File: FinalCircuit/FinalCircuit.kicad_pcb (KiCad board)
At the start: 2 copper layers, 163.3 x 78.7 mm, 54 parts, among them J1 Conn_02x20_Odd_Even, J2 Conn_02x05_Odd_Even, J3 Conn_01x06, U1 LM6172, U10 CD4066BE, U11 CD4066BE, U2 OPA2277, U3 MCP3008, U4 MCP4921, U5 CD4066BE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

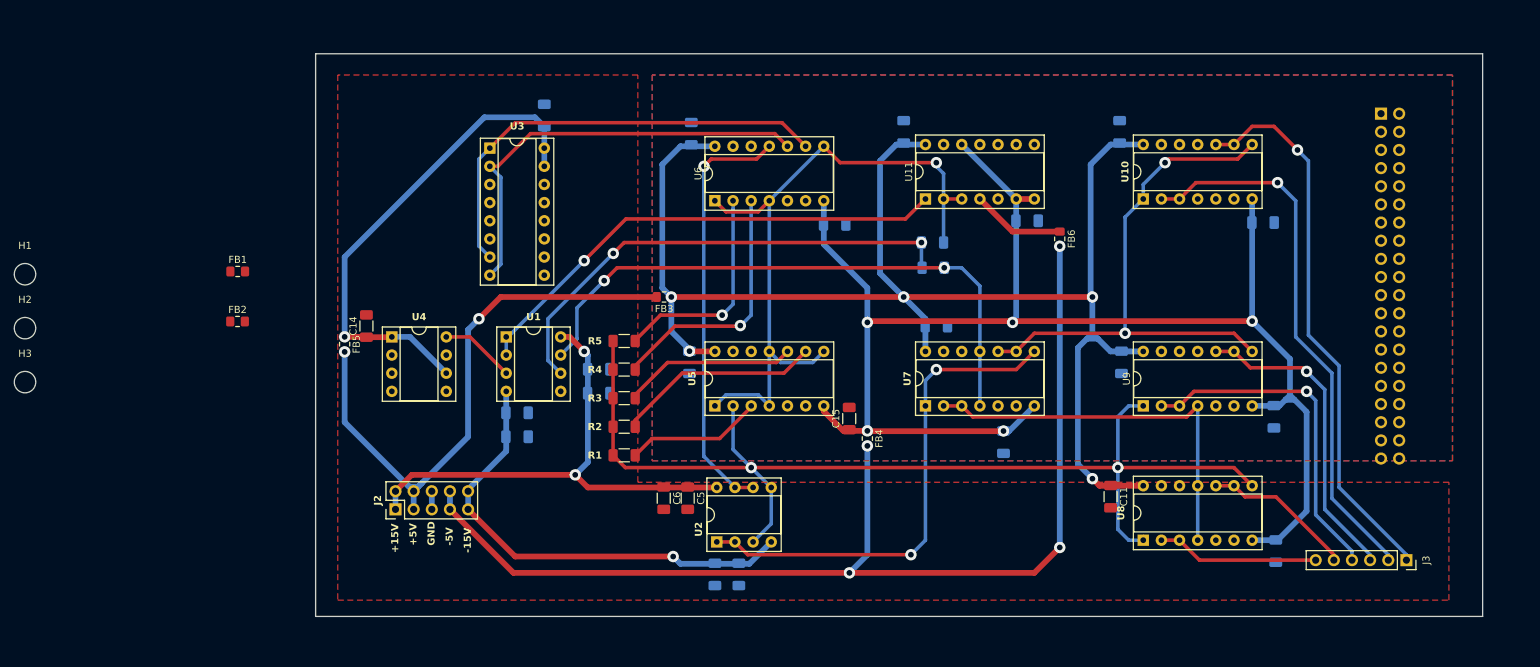
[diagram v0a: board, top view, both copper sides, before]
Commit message: Almost all connections done. Digital traces seem too long at the moment.
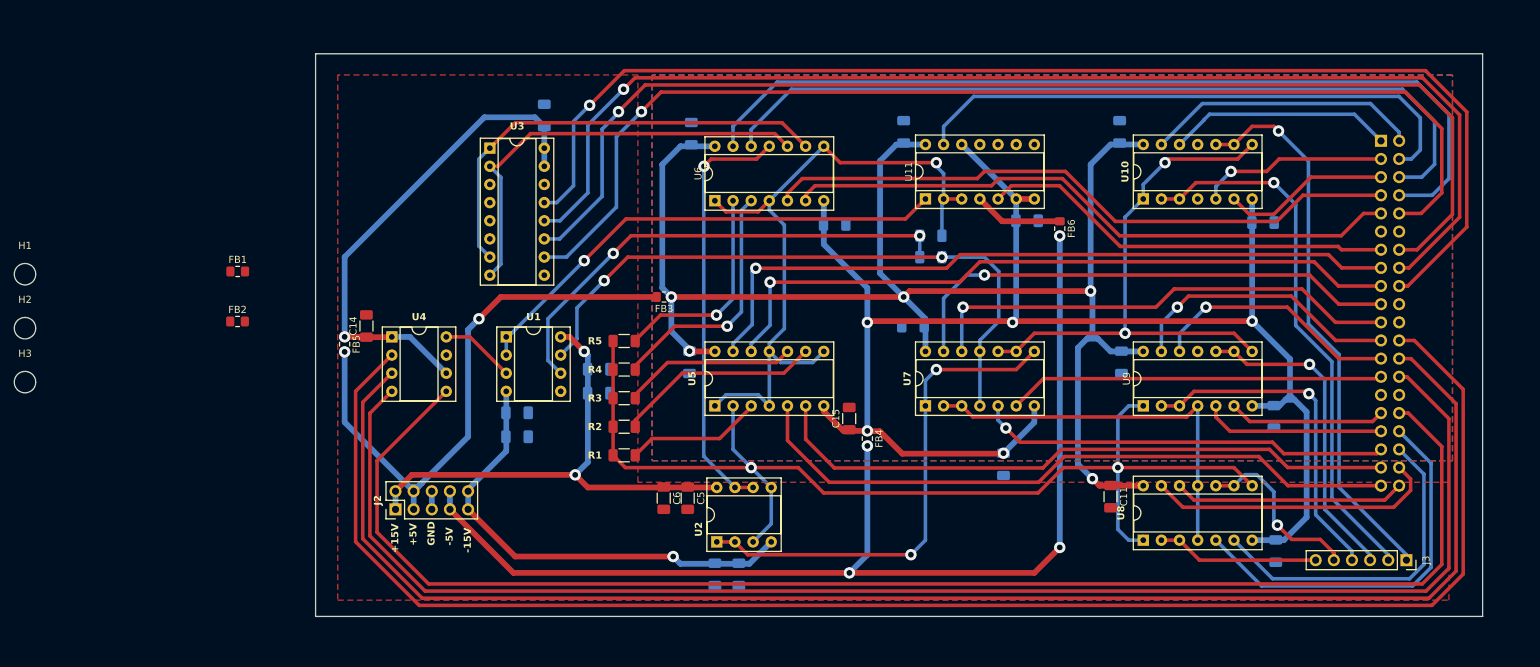
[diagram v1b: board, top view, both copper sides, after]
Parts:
- moved J1 3.80 mm to (238.0, 46.2)
- moved C9 3.27 mm to (172.5, 72.1), turned to 180 degrees
- moved C10 3.11 mm to (185.2, 91.5)
- moved R11 1.52 mm to (175.0, 62.5)
- moved FB6 1.44 mm to (193.0, 58.5)
- moved R10 0.98 mm to (175.0, 59.5)
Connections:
- J1 pad 1: /DAC_CSbar -> /Control_Vt2B
- J1 pad 10: /Control4 -> /ADC_CSbar
- J1 pad 13: /Control9A -> /ControlMain_Reset
- J1 pad 14: /Control5 -> /Din
- J1 pad 15: /Control10B -> /Control1
- J1 pad 16: /Control6 -> /Dout
- J1 pad 17: /Control9B -> /Control4
- J1 pad 18: /Control_Vt1A -> /CLK
- J1 pad 19: /Control10A -> /Control9A
- J1 pad 2: /SCK -> /Control_Vt1A
- J1 pad 20: /Control_Vt1B -> unconnected-(J1-Pin_20-Pad20)
- J1 pad 21: /Control_Hz1A -> /Control10B
- J1 pad 22: /Control_Vt2A -> unconnected-(J1-Pin_22-Pad22)
- J1 pad 23: /Control_Hz1B -> /Control_Hz3A
- J1 pad 24: /Control_Vt2B -> /DAC_CSbar
- J1 pad 25: /Control_Hz2A -> /Control_Vt3B
- J1 pad 26: /Control_Vt3A -> /SCK
- J1 pad 27: /Control_Hz2B -> /Control10A
- J1 pad 28: /Control_Vt3B -> /SDI
- J1 pad 3: /LDACbar -> /Control_Vt1B
- J1 pad 31: /Control_Hz3A -> /Control_Vt3A
- J1 pad 32: /Dout -> /LDACbar
- J1 pad 34: /ADC_CSbar -> /Control_Hz1B
- J1 pad 35: /ControlMain_ReadWrite -> /Control9B
- J1 pad 36: /Din -> /Control_Hz2A
- J1 pad 37: /ControlMain_Reset -> /Control3
- J1 pad 38: unconnected-(J1-Pin_38-Pad38) -> /Control_Hz1A
- J1 pad 39: /CLK -> /Control2
- J1 pad 4: /SDI -> /ControlMain_ReadWrite
- J1 pad 40: unconnected-(J1-Pin_40-Pad40) -> /Control_Hz2B
- J1 pad 5: /Control7 -> /Control_Vt2A
- J1 pad 6: /Control2 -> /Control8
- J1 pad 7: /Control8 -> /Control5
- J1 pad 8: /Control3 -> /Control6
- J1 pad 9: /Control1 -> /Control7
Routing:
- net /DAC_CSbar: track 0.00 -> 226.4 mm
- net /SCK: track 0.00 -> 216.9 mm
- net /SDI: track 0.00 -> 207.3 mm
- net /LDACbar: track 0.00 -> 201.3 mm
- net /CLK: track 0.00 -> 173.4 mm, vias 0 -> 1
- net /Dout: track 0.00 -> 169.8 mm, vias 0 -> 1
- net /Din: track 0.00 -> 166.5 mm, vias 0 -> 1
- net /ADC_CSbar: track 0.00 -> 159.2 mm, vias 0 -> 1
- net /Control6: track 0.00 -> 124.3 mm
- net /Control8: track 0.00 -> 113.9 mm
- net /Control1: track 0.00 -> 102.0 mm, vias 0 -> 1
- net /Control4: track 0.00 -> 98.9 mm, vias 0 -> 1
- net /Control2: track 0.00 -> 93.5 mm
- net /Control5: track 0.00 -> 89.8 mm
- net /Control3: track 0.00 -> 89.0 mm
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
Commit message: Final PCB all routing done, 0 errors. Verification left
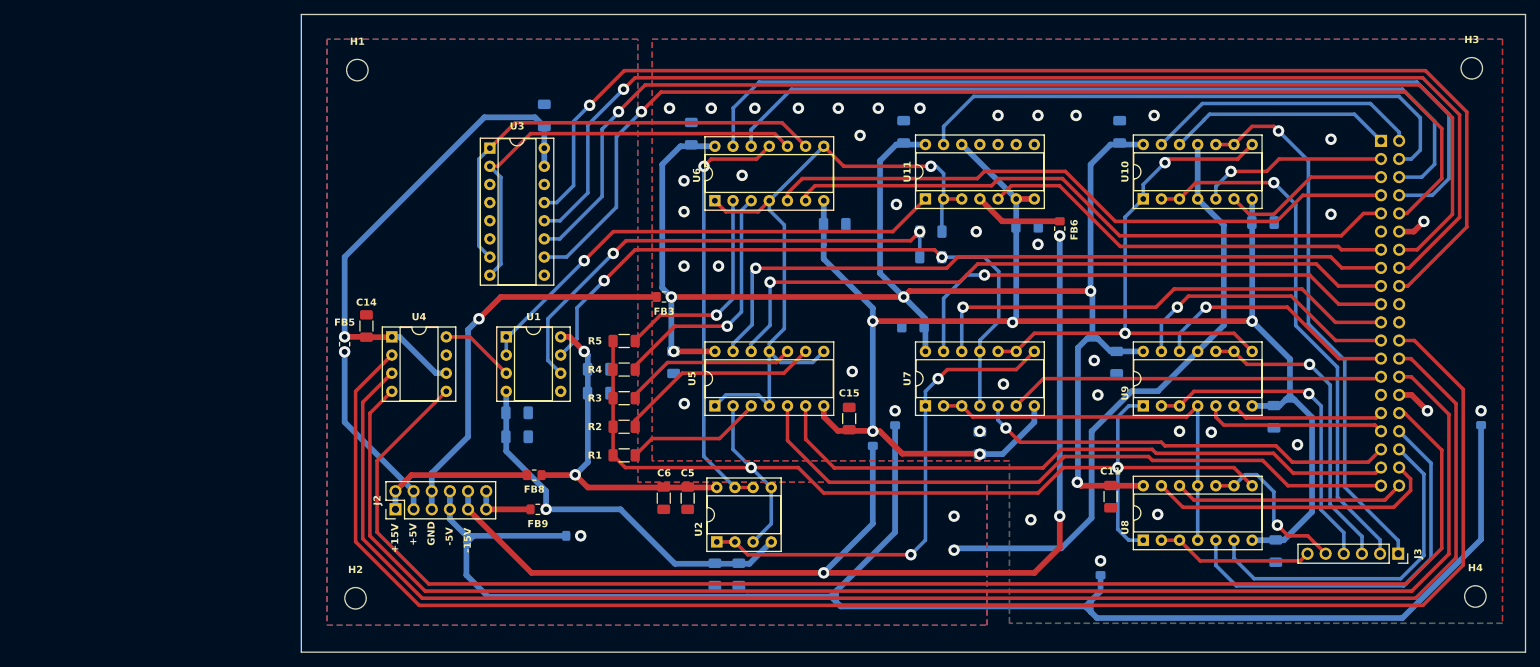
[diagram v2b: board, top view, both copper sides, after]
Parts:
- added FB10: FerriteBead, Inductor_SMD:L_0805_2012Metric_Pad1.15x1.40mm_HandSolder, B.Cu at (198.8, 106.0)
- added FB7: FerriteBead, Inductor_SMD:L_0805_2012Metric_Pad1.15x1.40mm_HandSolder, B.Cu at (252.0, 85.0)
- added FB8: FerriteBead, Inductor_SMD:L_0805_2012Metric_Pad1.15x1.40mm_HandSolder, F.Cu at (119.5, 93.0)
- added FB9: FerriteBead, Inductor_SMD:L_0805_2012Metric_Pad1.15x1.40mm_HandSolder, F.Cu at (120.0, 97.8)
- added H4: MountingHole, MountingHole:MountingHole_3mm, F.Cu at (251.2, 110.0)
- FB1, FB2, FB4: moved to B.Cu
- J2: value Conn_02x05_Odd_Even -> Conn_02x06_Odd_Even; footprint Connector_PinHeader_2.54mm:PinHeader_2x05_P2.54mm_Vertical -> Connector_PinHeader_2.54mm:PinHeader_2x06_P2.54mm_Vertical
- moved H3 207.2 mm to (250.7, 36.1)
- moved FB1 94.3 mm to (170.0, 85.0), turned to -90 degrees
- moved H2 59.7 mm to (94.5, 110.2)
- moved FB2 55.8 mm to (125.0, 101.5), turned to 180 degrees
- moved H1 54.6 mm to (94.7, 36.3)
- moved C10 4.46 mm to (181.9, 88.5), turned to 90 degrees
- moved C16 2.22 mm to (139.0, 77.2)
- moved J3 1.46 mm to (240.4, 104.0)
- moved C24 0.76 mm to (188.5, 58.2)
- moved FB4 0.76 mm to (166.9, 87.9)
- moved C19 0.68 mm to (201.0, 77.2)
- moved R10 0.57 mm to (175.0, 58.9)
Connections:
- net /+5VD renamed /+SwitchD
- C1 pad 1: /+15V -> /+15VA
- C2 pad 1: /+15V -> /+15VA
- C3 pad 1: /-15V -> /-15VA
- C4 pad 1: /-15V -> /-15VA
- C5 pad 1: /+15V -> /+15VA
- C6 pad 1: /+15V -> /+15VA
- C7 pad 1: /-15V -> /-15VA
- C8 pad 1: /-15V -> /-15VA
- FB3 pad 2: /+5V -> /+Switch
- J2 pad 10: /-15V -> /-5V
- J2 pad 5: /PowerGND -> /+Switch
- J2 pad 6: /PowerGND -> /+Switch
- J2 pad 7: /-5V -> /PowerGND
- J2 pad 8: /-5V -> /PowerGND
- J2 pad 9: /-15V -> /-5V
- U1 pad 4: /-15V -> /-15VA
- U1 pad 8: /+15V -> /+15VA
- U2 pad 4: /-15V -> /-15VA
- U2 pad 8: /+15V -> /+15VA
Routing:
- net /PowerGND: track 2.54 -> 229.4 mm
- net GNDA: track 0.00 -> 84.7 mm, vias 0 -> 3
- net /-15V: track 65.6 -> 8.75 mm, vias 1 -> 0
- net /+5V: track 82.5 -> 26.0 mm, vias 2 -> 1
- net /+Switch: track 0.00 -> 55.6 mm, vias 0 -> 1
- net /-15VA: track 0.00 -> 54.7 mm, vias 0 -> 1
- net /+15V: track 71.5 -> 21.9 mm, vias 2 -> 0
- net /+15VA: track 0.00 -> 47.6 mm, vias 0 -> 2
- net GNDD: track 0.00 -> 8.93 mm, vias 0 -> 38
- net /+SwitchD: track 206.8 -> 209.7 mm
- net /Hz2: track 25.1 -> 23.0 mm
- net /LDACbar: track 201.3 -> 199.7 mm
- net /Control6: track 124.3 -> 125.8 mm
- net /Hz3: track 47.4 -> 46.0 mm
- net /Vt2: track 77.6 -> 76.2 mm
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- added copper zone on B.Cu, net GNDA
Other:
- board size 163.3 x 78.7 mm -> 171.3 x 89.2 mm

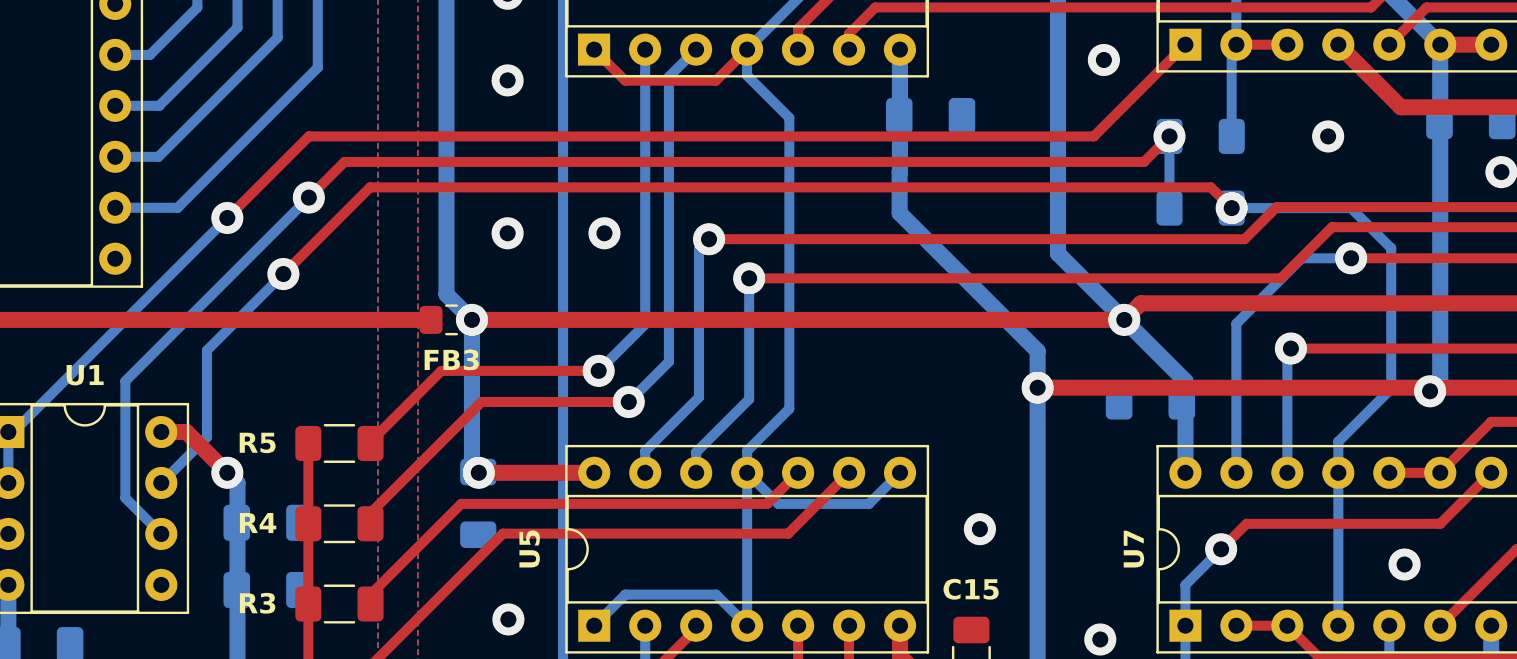
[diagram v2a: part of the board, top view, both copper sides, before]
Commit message: Found an error in LM6172 connection. Routing of that is left.
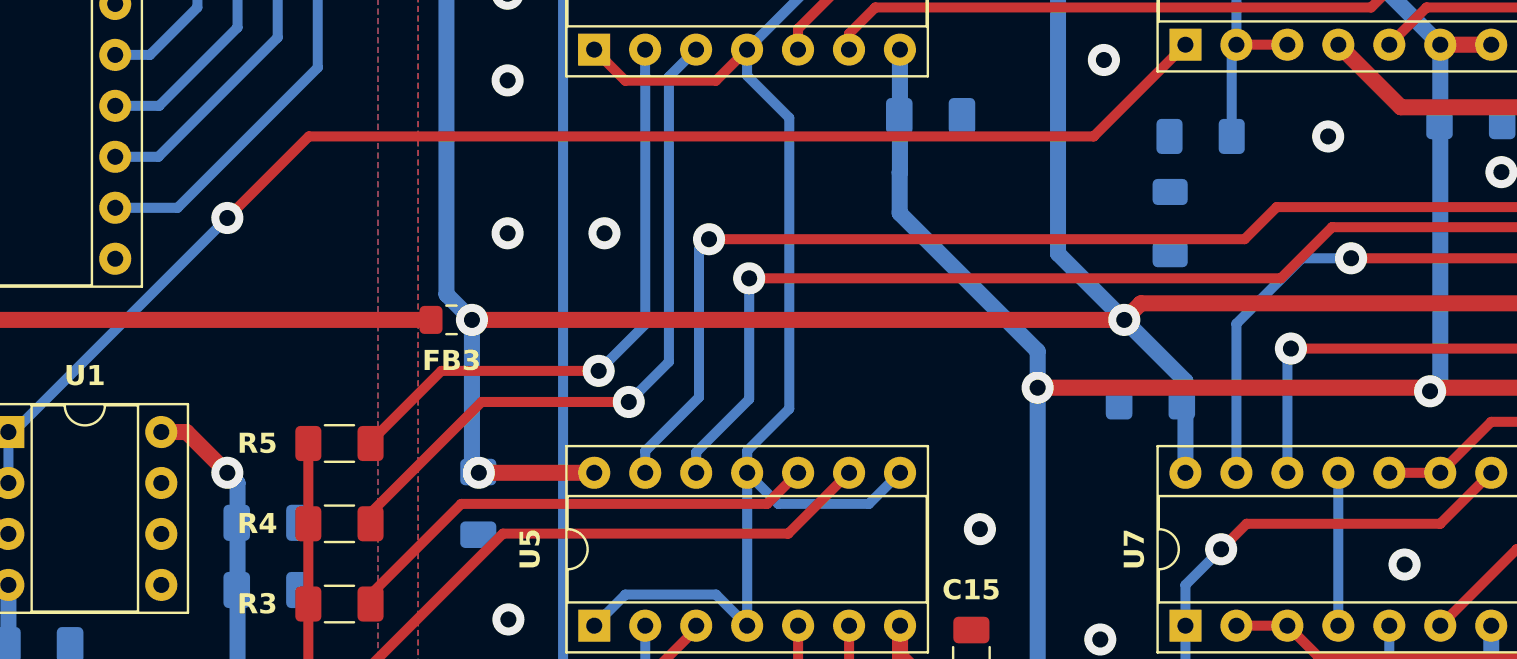
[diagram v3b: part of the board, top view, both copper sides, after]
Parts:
- removed R11: 10k, Resistor_SMD:R_1206_3216Metric_Pad1.30x1.75mm_HandSolder
- added R6: 10k, Resistor_SMD:R_1206_3216Metric_Pad1.30x1.75mm_HandSolder, B.Cu at (173.5, 63.2)
- R10: value 20k -> 10k
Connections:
- R10 pad 2: /Write_FB -> Net-(U1B-+)
- U1 pad 5: GNDA -> Net-(U1B-+)
- U1 pad 6: /Write_FB -> /S10inB
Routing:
- net /S10inB: track 91.1 -> 7.62 mm, vias 2 -> 0
- net /Write_FB: track 69.0 -> 0.00 mm, vias 2 -> 0

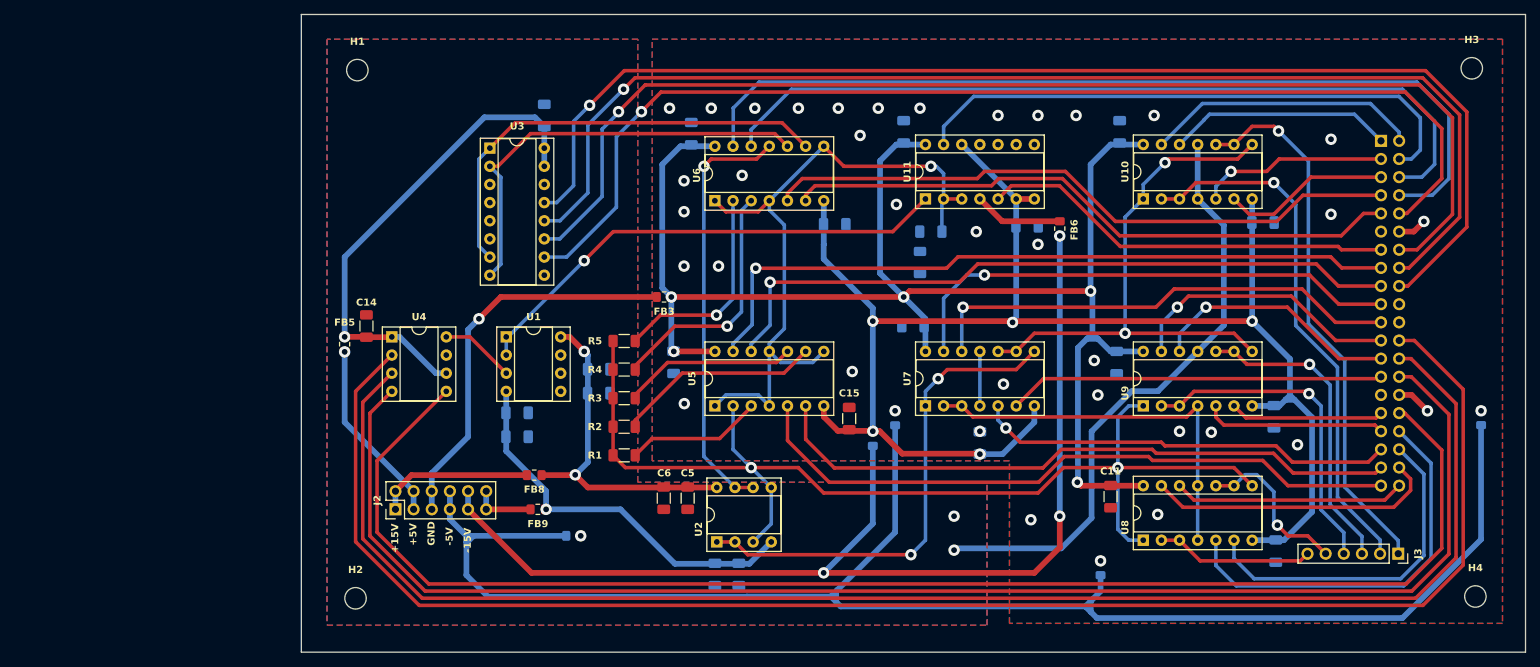
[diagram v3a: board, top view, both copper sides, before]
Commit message: Final PCB Done. Resistive Crossbar PCB Done. Verification left.
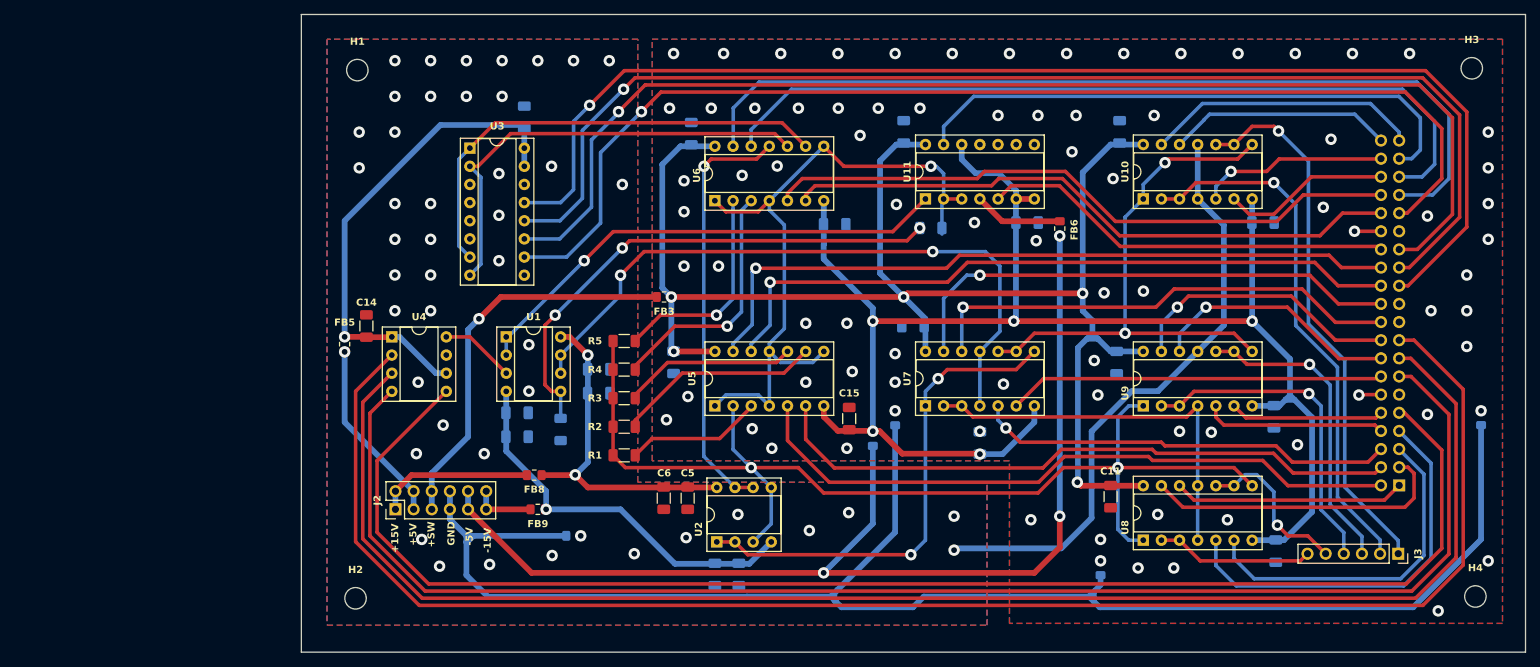
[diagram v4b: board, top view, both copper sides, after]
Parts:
- moved R6 55.5 mm to (123.2, 86.6)
- moved J1 48.3 mm to (240.5, 94.4), turned to 0 degrees
- moved C13 2.81 mm to (118.1, 42.9)
- moved U3 2.79 mm to (110.5, 47.2)
- moved C24 0.51 mm to (188.5, 57.7)
- moved R10 0.51 mm to (175.0, 58.4)
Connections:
- net /S10inA renamed /Read_FB
- J1 pad 1: /Control_Vt2B -> /Control_Hz2B
- J1 pad 10: /ADC_CSbar -> /Control_Vt3A
- J1 pad 13: /ControlMain_Reset -> /SDI
- J1 pad 14: /Din -> /Control10A
- J1 pad 15: /Control1 -> /SCK
- J1 pad 16: /Dout -> /Control_Vt3B
- J1 pad 17: /Control4 -> /DAC_CSbar
- J1 pad 18: /CLK -> /Control_Hz3A
- J1 pad 19: /Control9A -> unconnected-(J1-Pin_19-Pad19)
- J1 pad 2: /Control_Vt1A -> /Control2
- J1 pad 20: unconnected-(J1-Pin_20-Pad20) -> /Control10B
- J1 pad 21: /Control10B -> unconnected-(J1-Pin_21-Pad21)
- J1 pad 22: unconnected-(J1-Pin_22-Pad22) -> /Control9A
- J1 pad 23: /Control_Hz3A -> /CLK
- J1 pad 24: /DAC_CSbar -> /Control4
- J1 pad 25: /Control_Vt3B -> /Dout
- J1 pad 26: /SCK -> /Control1
- J1 pad 27: /Control10A -> /Din
- J1 pad 28: /SDI -> /ControlMain_Reset
- J1 pad 3: /Control_Vt1B -> /Control_Hz1A
- J1 pad 31: /Control_Vt3A -> /ADC_CSbar
- J1 pad 32: /LDACbar -> /Control7
- J1 pad 33: /Control_Hz3B -> /Control6
- J1 pad 34: /Control_Hz1B -> /Control5
- J1 pad 35: /Control9B -> /Control8
- J1 pad 36: /Control_Hz2A -> /Control_Vt2A
- J1 pad 37: /Control3 -> /ControlMain_ReadWrite
- J1 pad 38: /Control_Hz1A -> /Control_Vt1B
- J1 pad 39: /Control2 -> /Control_Vt1A
- J1 pad 4: /ControlMain_ReadWrite -> /Control3
- J1 pad 40: /Control_Hz2B -> /Control_Vt2B
- J1 pad 5: /Control_Vt2A -> /Control_Hz2A
- J1 pad 6: /Control8 -> /Control9B
- J1 pad 7: /Control5 -> /Control_Hz1B
- J1 pad 8: /Control6 -> /Control_Hz3B
- J1 pad 9: /Control7 -> /LDACbar
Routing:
- net /S10inB: track 7.62 -> 93.2 mm, vias 0 -> 2
- net Net-(U1B-+): track 0.00 -> 72.8 mm, vias 0 -> 3
- net /CLK: track 173.4 -> 176.5 mm
- net /S8out: track 60.8 -> 63.6 mm
- net /S7out: track 63.6 -> 66.3 mm
- net /Dout: track 169.8 -> 172.6 mm
- net /Din: track 166.5 -> 169.3 mm
- net /ADC_CSbar: track 158.0 -> 160.8 mm
- net GNDD: track 8.93 -> 6.83 mm, vias 38 -> 82
- net /Control_Hz1A: track 41.0 -> 43.0 mm
- net /-5VD: track 220.9 -> 222.4 mm
- net /PowerGND: track 229.4 -> 227.9 mm
- net /+5VA: track 69.7 -> 68.8 mm
- net GNDA: vias 3 -> 45
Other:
- board text added: "+SW"
